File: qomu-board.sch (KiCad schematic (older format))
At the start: 34 parts, among them IC1 EOS-S3, SW2 Captouch Pads, U1 LDO-X2SON-1.2V, U10 RGB-LED, U2 LDO-X2SON-3.3V, U3 LDO-X2SON-2.5V, U4 GD25Q16CEIGR, U5 MC3635, U9 USB-B

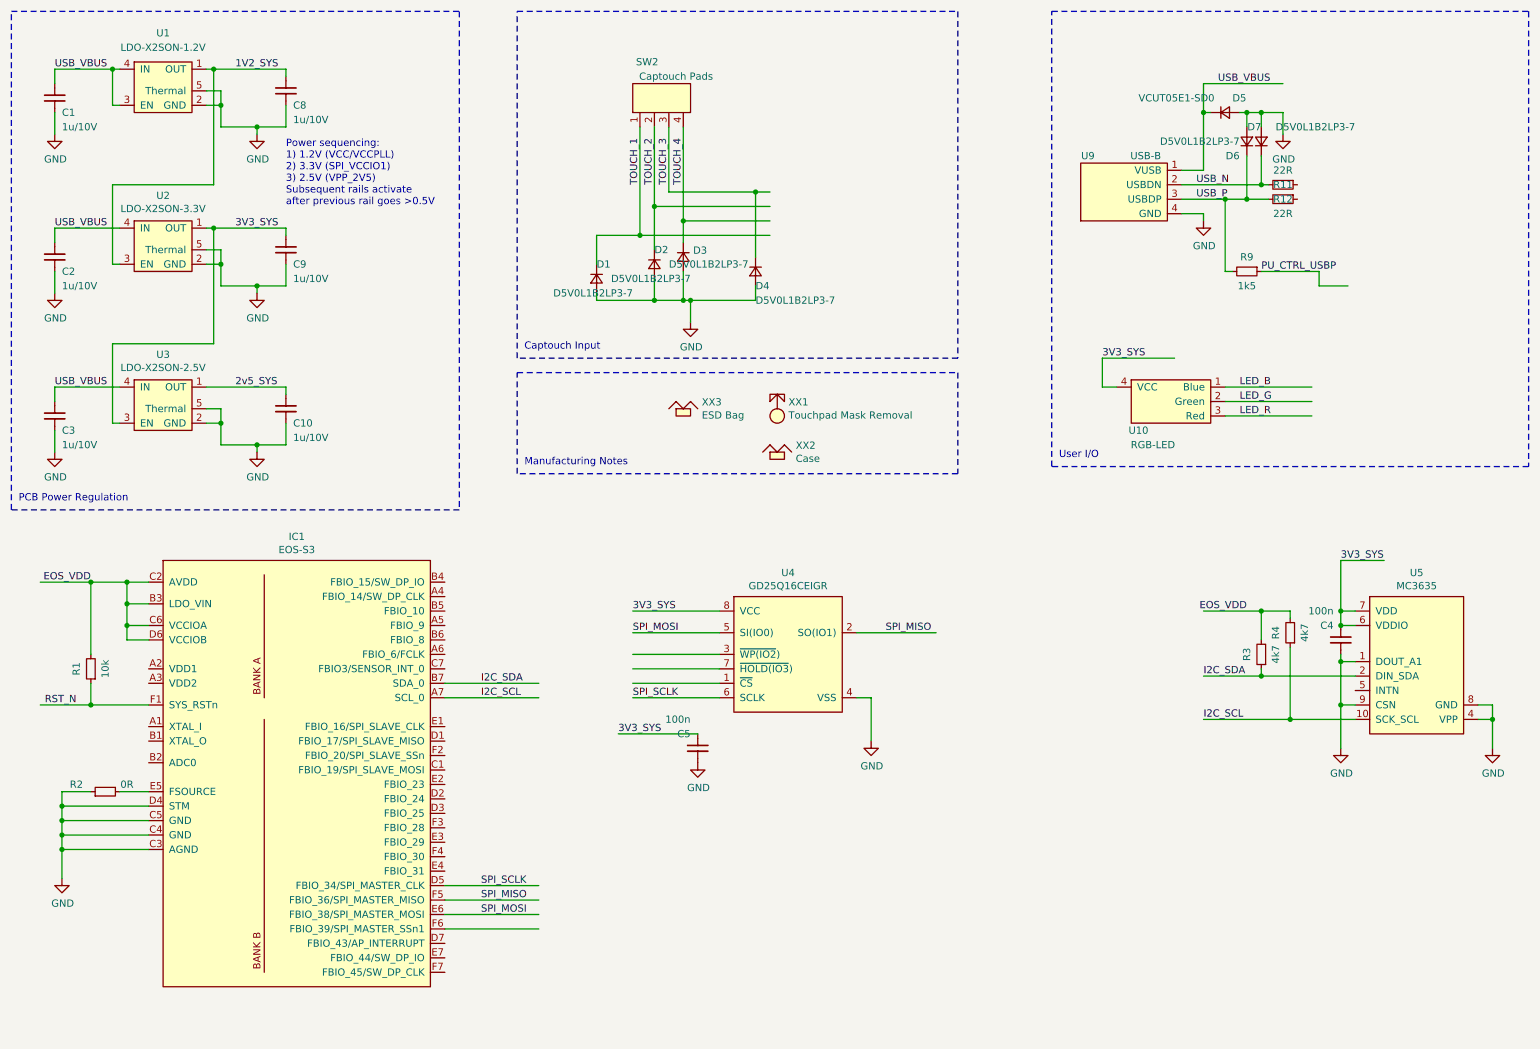
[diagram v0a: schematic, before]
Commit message: Connected missing nets, schematic cleanup
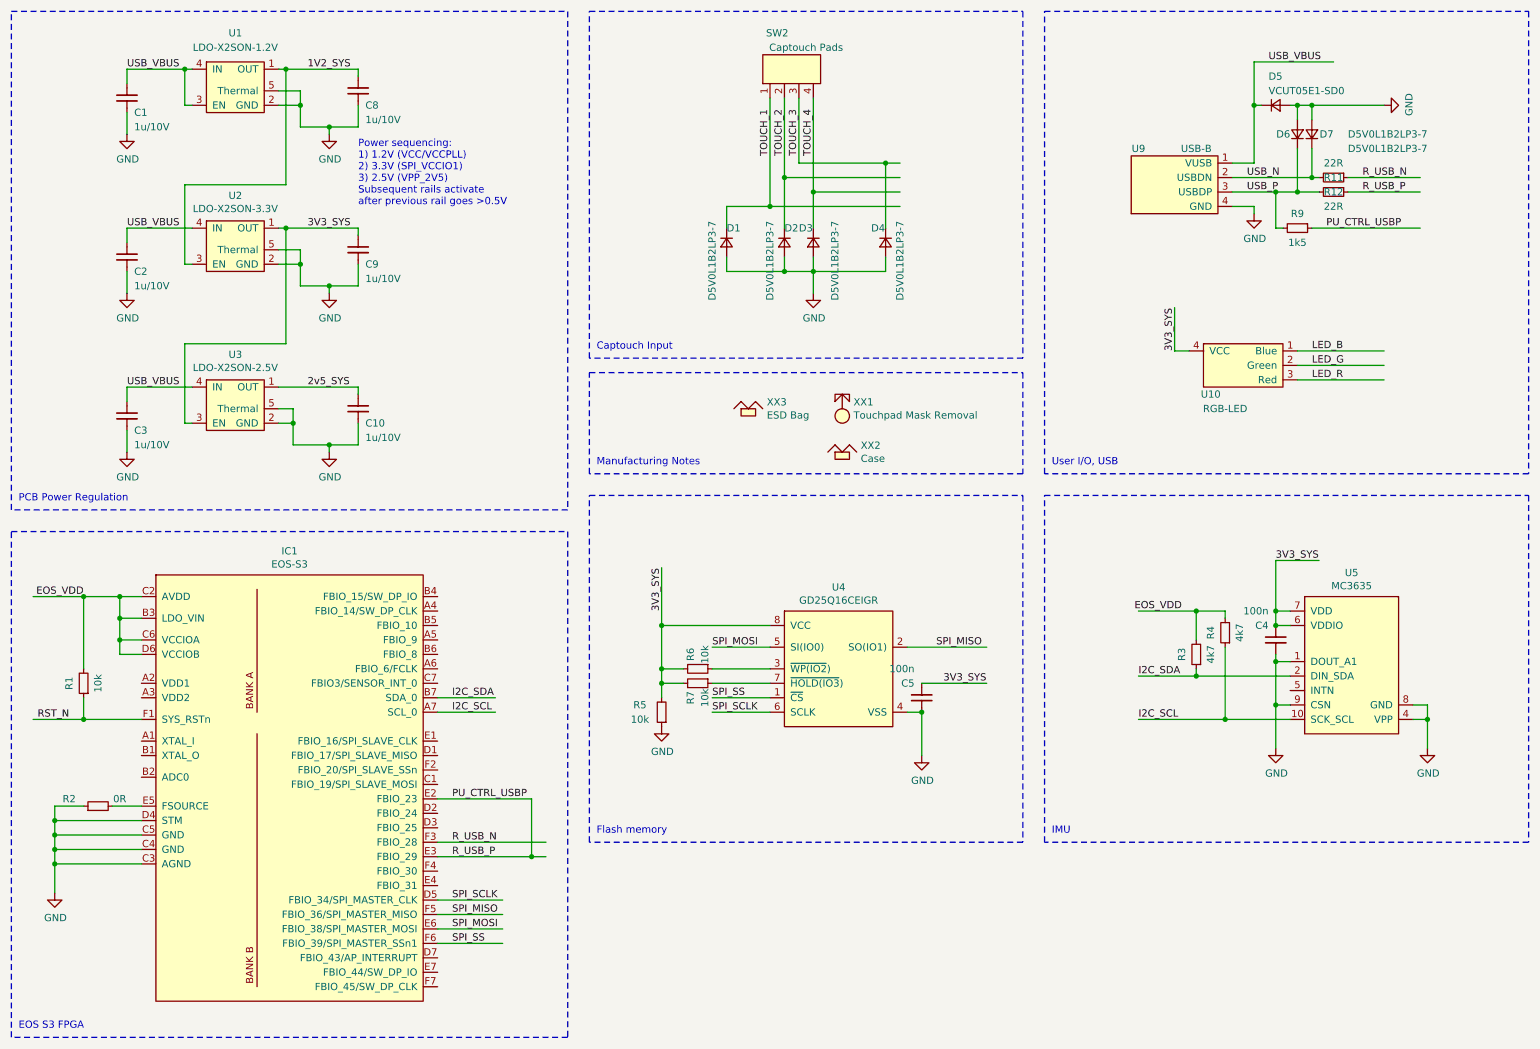
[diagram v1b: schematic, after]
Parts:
- added R5, R6, R7: 10k, qomu-board:R_0201_0603Metric, symbol qomu-board:R_Small-Device
- U5: footprint antmicro-footprints:MC3635 -> qomu-board:MC3635
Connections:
- net labels added: R_USB_N, R_USB_P, SPI_SS
- wire segments 170 -> 178
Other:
- note added: "EOS S3 FPGA"
- note added: "Flash memory"
- note added: "IMU"
- note added: "User I/O, USB"
- note removed: "User I/O"
- moved on the sheet: C1, C10, C2, C3, C4, C5, C8, C9, D1, D2, D3, D4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

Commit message: Fixed USB_D_P pull-up connection, tied U5 CS pin to VDDIO, added some remarks on schematics
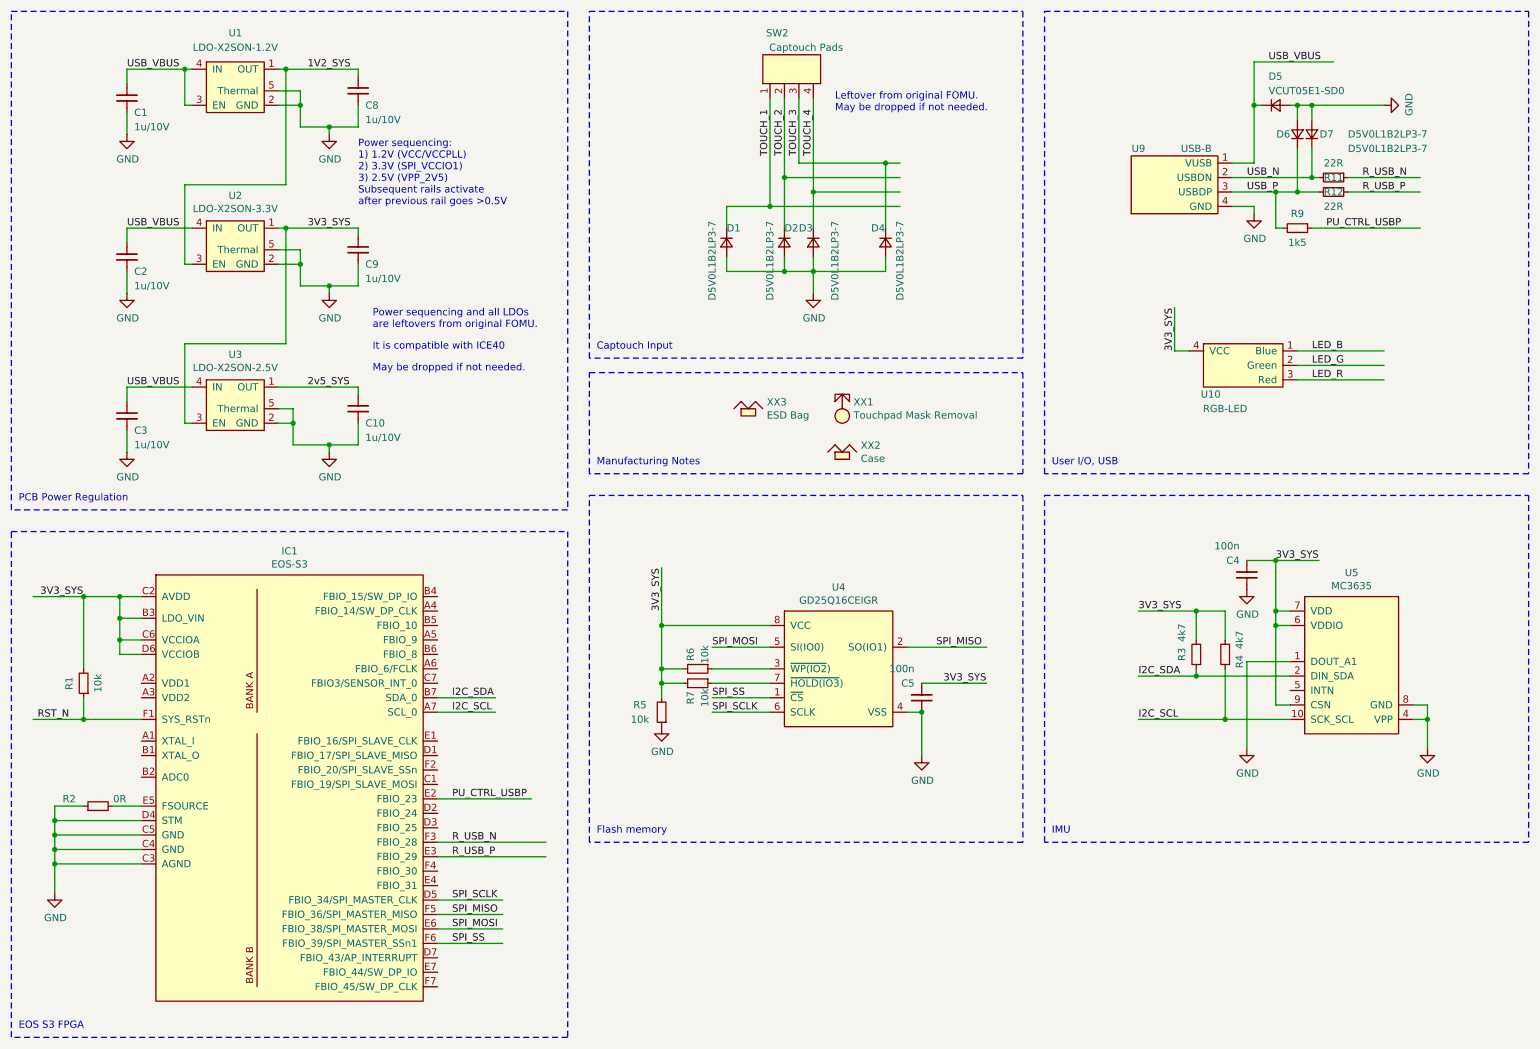
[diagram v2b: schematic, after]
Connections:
- net labels removed: EOS_VDD
- wire segments 178 -> 176
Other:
- note added: "It is compatible with ICE40"
- note added: "Leftover from original FOMU. \nMay be dropped if not needed."
- note added: "May be dropped if not needed."
- note added: "Power sequencing and all LDOs\nare leftovers from original FOMU.\n"
- moved on the sheet: C4, R4
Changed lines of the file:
@@
 EESchema Schematic File Version 4
 LIBS:qomu-board-cache
-EELAYER 26 0
+EELAYER 30 0
 EELAYER END
 $Descr A4 11693 8268
@@
 Wire Wire Line
 	1500 4650 1350 4650
-Text Label 1100 4650 2    50   ~ 0
-EOS_VDD
 Wire Wire Line
 	1500 4800 1350 4800
@@
 	9450 5200 8800 5200
 Wire Wire Line
-	9450 5500 9000 5500
-Wire Wire Line
 	9350 4750 9350 4400
 Wire Wire Line
 	9350 4400 9650 4400
 Connection ~ 9350 4750
-Wire Wire Line
-	9450 5400 9350 5400
-Wire Wire Line
-	9350 5400 9350 5700
 $Comp
 L power:GND #PWR05
 U 1 1 5DDB8FF0
-P 9350 5700
-F 0 "#PWR05" H 9350 5450 50  0001 C CNN
-F 1 "GND" H 9355 5527 50  0000 C CNN
-F 2 "" H 9350 5700 50  0001 C CNN
-F 3 "" H 9350 5700 50  0001 C CNN
-	1    9350 5700
-	1    0    0    -1
-$EndComp
-Wire Wire Line
-	9450 5100 9350 5100
-Wire Wire Line
-	9350 5100 9350 5400
-Connection ~ 9350 5400
+P 9150 5700
+F 0 "#PWR05" H 9150 5450 50  0001 C CNN
+F 1 "GND" H 9155 5527 50  0000 C CNN
+F 2 "" H 9150 5700 50  0001 C CNN
+F 3 "" H 9150 5700 50  0001 C CNN
+	1    9150 5700
+	1    0    0    -1
+$EndComp
 Wire Wire Line
 	3550 5350 3950 5350
@@
 Text Label 8400 5500 0    50   ~ 0
 I2C_SCL
-Text Label 8700 4750 2    50   ~ 0
-EOS_VDD
-Text Label 9350 4400 0    50   ~ 0
-3V3_SYS
 Wire Wire Line
 	8800 5200 8800 5150
@@
 P 8800 5050
 F 0 "R3" V 8900 5050 50  0000 C CNN
-F 1 "4k7" V 8700 5050 50  0000 C CNN
+F 1 "4k7" V 8900 4900 50  0000 C CNN
 F 2 "qomu-board:R_0201_0603Metric" H 8800 5050 50  0001 C CNN
 F 3 "" H 8800 5050 50  0001 C CNN
@@
 L qomu-board:R_Small-Device R4
 U 1 1 5DDF069C
-P 9000 4900
-F 0 "R4" V 9100 4900 50  0000 C CNN
-F 1 "4k7" V 8900 4900 50  0000 C CNN
-F 2 "qomu-board:R_0201_0603Metric" H 9000 4900 50  0001 C CNN
-F 3 "" H 9000 4900 50  0001 C CNN
-F 4 "ANY" H 250 3200 50  0001 C CNN "MPN"
-	1    9000 4900
+P 9000 5050
+F 0 "R4" V 8900 5100 50  0000 C CNN
+F 1 "4k7" V 8900 4950 50  0000 C CNN
+F 2 "qomu-board:R_0201_0603Metric" H 9000 5050 50  0001 C CNN
+F 3 "" H 9000 5050 50  0001 C CNN
+F 4 "ANY" H 250 3350 50  0001 C CNN "MPN"
+	1    9000 5050
 	-1   0    0    1
 $EndComp
 Wire Wire Line
-	9000 5000 9000 5500
-Wire Wire Line
 	8800 4950 8800 4750
 Wire Wire Line
 	8800 4750 9000 4750
-Wire Wire Line
-	9000 4750 9000 4800
-$Comp
-L qomu-board:C_Small-Device C4
-U 1 1 5DE4FACB
-P 9350 4950
-F 0 "C4" H 9400 4850 50  0000 L CNN
-F 1 "100n" H 9400 4750 50  0000 L CNN
-F 2 "qomu-board:C_0201_0603Metric" H 9350 4950 50  0001 C CNN
-F 3 "" H 9350 4950 50  0001 C CNN
-	1    9350 4950
-	-1   0    0    1
-$EndComp
-Connection ~ 9350 4850
-Wire Wire Line
-	9350 5050 9350 5100
-Connection ~ 9350 5100
 Wire Wire Line
 	8800 4750 8400 4750
@@
 	8800 5200 8400 5200
 Connection ~ 8800 5200
-Wire Wire Line
-	9000 5500 8400 5500
-Connection ~ 9000 5500
 Text Label 5450 5000 0    50   ~ 0
 SPI_MOSI
@@
 R_USB_P
 Wire Wire Line
-	4200 6050 4200 6450
-Wire Wire Line
 	3550 6050 4200 6050
-Wire Wire Line
-	3550 6450 4200 6450
-Connection ~ 4200 6450
-Wire Wire Line
-	4200 6450 4300 6450
 Wire Wire Line
 	3550 6350 4300 6350
@@
 	1    0    0    -1
 $EndComp
+Wire Wire Line
+	3550 6450 4300 6450
+Text Notes 6300 1300 0    50   ~ 0
+Leftover from original FOMU. \nMay be dropped if not needed.
+Text Label 9350 4400 0    50   ~ 0
+3V3_SYS
+Text Label 8400 4750 0    50   ~ 0
+3V3_SYS
+Text Label 800  4650 0    50   ~ 0
+3V3_SYS
+Text Notes 3100 2800 0    50   ~ 0
+Power sequencing and all LDOs\nare leftovers from original FOMU.\n
+Text Notes 3100 3100 0    50   ~ 0
+May be dropped if not needed.
+$Comp
+L qomu-board:C_Small-Device C4
+U 1 1 5DE4FACB
+P 9150 4500
+F 0 "C4" H 9200 4400 50  0000 L CNN
+F 1 "100n" H 9200 4300 50  0000 L CNN
+F 2 "qomu-board:C_0201_0603Metric" H 9150 4500 50  0001 C CNN
+F 3 "" H 9150 4500 50  0001 C CNN
+	1    9150 4500
+	-1   0    0    1
+$EndComp
+Wire Wire Line
+	9450 5100 9150 5100
+Wire Wire Line
+	9150 5100 9150 5700
+Wire Wire Line
+	9450 5400 9350 5400
+Wire Wire Line
+	9350 5400 9350 4850
+Connection ~ 9350 4850
+Wire Wire Line
+	9350 4400 9150 4400
+Connection ~ 9350 4400
+$Comp
+L power:GND #PWR?
+U 1 1 5DEB67F5
+P 9150 4600
+F 0 "#PWR?" H 9150 4350 50  0001 C CNN
+F 1 "GND" H 9155 4427 50  0000 C CNN
+F 2 "" H 9150 4600 50  0001 C CNN
+F 3 "" H 9150 4600 50  0001 C CNN
+	1    9150 4600
+	1    0    0    -1
+$EndComp
+Wire Wire Line
+	8400 5500 9000 5500
+Wire Wire Line
+	9000 4750 9000 4950
+Wire Wire Line
+	9000 5150 9000 5500
+Connection ~ 9000 5500
+Wire Wire Line
+	9000 5500 9450 5500
+Text Notes 3100 2950 0    50   ~ 0
+It is compatible with ICE40
 $EndSCHEMATC

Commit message: Updated README
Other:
- note added: "EOS S3"
- note added: "Power sequencing and all LDOs\ninherited from FOMU design.\nNeed to be updated\n"
- note added: "Power supplies"
- note removed: "EOS S3 FPGA"
- note removed: "It is compatible with ICE40"
- note removed: "May be dropped if not needed."
- note removed: "PCB Power Regulation"
- note removed: "Power sequencing and all LDOs\nare leftovers from original FOMU.\n"
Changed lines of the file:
@@
 Date ""
 Rev ""
-Comp ""
+Comp "Antmicro Ltd. (www.antmicro.com)"
 Comment1 ""
 Comment2 ""
@@
 	600  4050 600  600
 Text Notes 650  4000 0    50   ~ 0
-PCB Power Regulation
+Power supplies
 Wire Notes Line
 	11100 3800 7750 3800
@@
 IMU
 Text Notes 650  7650 0    50   ~ 0
-EOS S3 FPGA
+EOS S3
 $Comp
 L qomu-board:MC3635 U5
@@
 Text Label 800  4650 0    50   ~ 0
 3V3_SYS
-Text Notes 3100 2800 0    50   ~ 0
-Power sequencing and all LDOs\nare leftovers from original FOMU.\n
-Text Notes 3100 3100 0    50   ~ 0
-May be dropped if not needed.
+Text Notes 3050 2950 0    50   ~ 0
+Power sequencing and all LDOs\ninherited from FOMU design.\nNeed to be updated\n
 $Comp
 L qomu-board:C_Small-Device C4
@@
 Wire Wire Line
 	9000 5500 9450 5500
-Text Notes 3100 2950 0    50   ~ 0
-It is compatible with ICE40
 $EndSCHEMATC

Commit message: Updated naming
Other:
- note added: "Accelerometer"
- note removed: "IMU"
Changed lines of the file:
@@
 Flash memory
 Text Notes 7800 6300 0    50   ~ 0
-IMU
+Accelerometer
 Text Notes 650  7650 0    50   ~ 0
 EOS S3
